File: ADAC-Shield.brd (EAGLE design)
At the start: 100 x 80 mm, 58 parts, among them U1 ARDUINO-MEGAFULL, U2 LM358D

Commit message: Some progress in PCB layout
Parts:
- removed R1: 0, rcl:R1206
- added JP4: (no value), pinhead:1X02
- moved C21 52.9 mm to (41.3, 26.0), turned to 270 degrees
- moved C25 50.7 mm to (52.1, 21.9), turned to 90 degrees
- moved R17 48.8 mm to (38.1, 22.5)
- moved C19 47.5 mm to (47.6, 31.4), turned to 270 degrees
- moved R19 45.3 mm to (57.8, 21.9), turned to 90 degrees
- moved C26 44.3 mm to (54.9, 21.6), turned to 90 degrees
- moved C23 41.9 mm to (52.7, 31.4), turned to 90 degrees
- moved C20 34.9 mm to (38.4, 26.0), turned to 270 degrees
- moved R18 34.9 mm to (58.4, 31.4), turned to 90 degrees
- moved C24 33.3 mm to (55.6, 31.8), turned to 270 degrees
- moved C22 28.0 mm to (44.8, 31.8), turned to 270 degrees
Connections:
- net +3V3: now also JP4.2; no longer R1.1
- net V+: now also JP4.1; no longer R1.2
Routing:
- net GND: track 54.6 -> 192.5 mm, vias 0 -> 2
- net V+: track 6.06 -> 46.9 mm, vias 0 -> 4
- net RIGHT_PREAMP_OUT: track 3.41 -> 17.9 mm, vias 0 -> 1
- net LEFT_PREAMP_OUT: track 3.41 -> 17.4 mm, vias 0 -> 1
- net N$19: track 0.00 -> 11.6 mm
- net N$20: track 0.00 -> 8.86 mm
- net N$25: track 0.00 -> 8.36 mm
- net N$18: track 0.00 -> 6.69 mm
- net +3V3: track 0.00 -> 2.86 mm, vias 0 -> 1

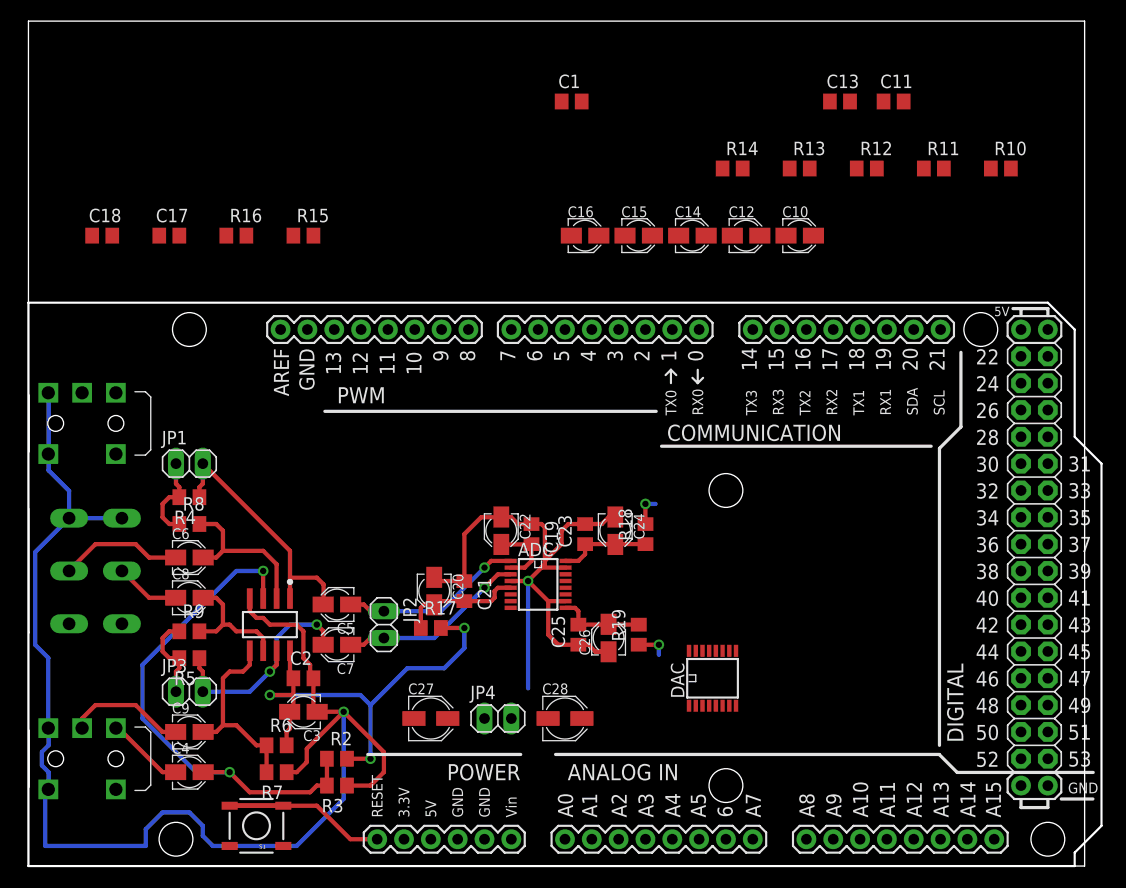
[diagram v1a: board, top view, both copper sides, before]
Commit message: PCB layout almost done
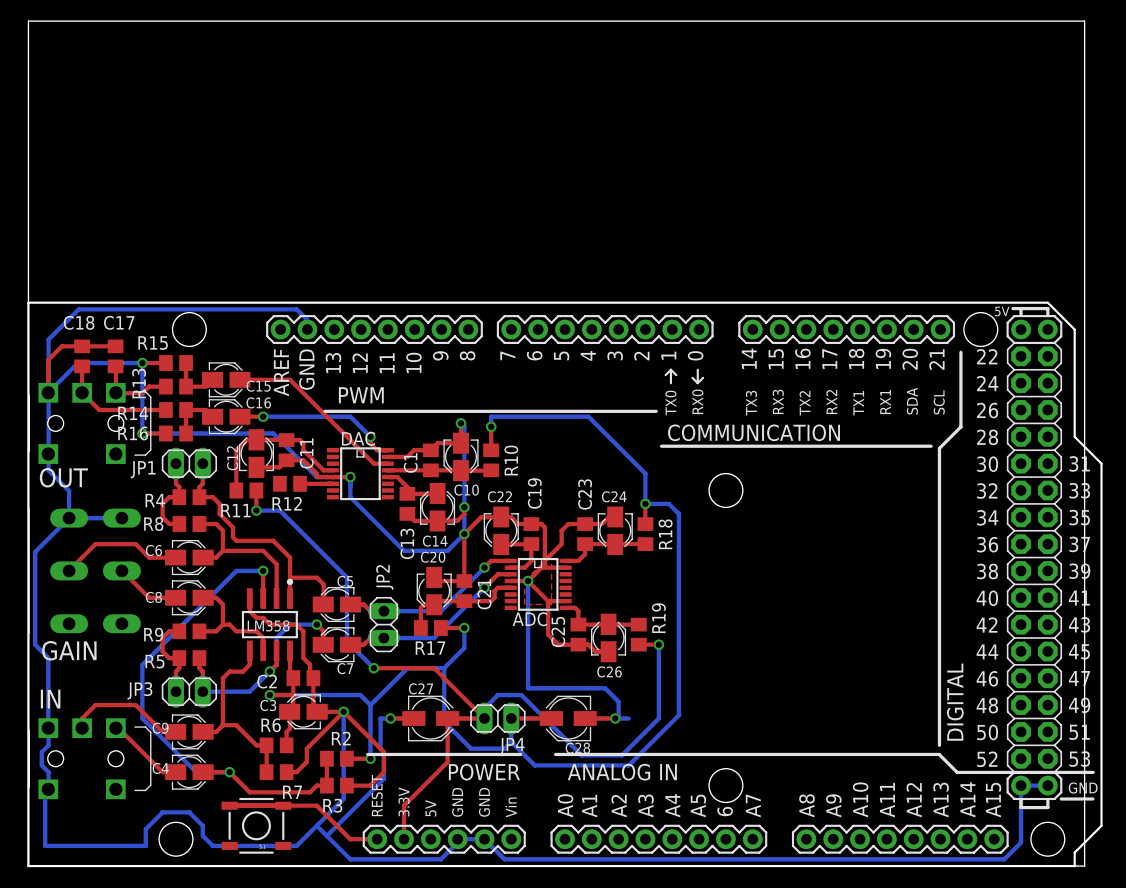
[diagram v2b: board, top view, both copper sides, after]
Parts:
- moved R11 71.9 mm to (20.6, 35.6)
- moved C11 66.3 mm to (24.4, 39.4), turned to 270 degrees
- moved R13 62.6 mm to (14.0, 45.4)
- moved R12 62.2 mm to (24.8, 36.2), turned to 180 degrees
- moved R14 57.4 mm to (14.0, 43.2)
- moved C13 55.9 mm to (35.9, 34.3), turned to 270 degrees
- moved R10 55.6 mm to (43.8, 38.4), turned to 90 degrees
- moved C12 50.7 mm to (21.6, 39.1), turned to 90 degrees
- moved C15 41.4 mm to (18.7, 46.0)
- moved DAC 38.6 mm to (31.4, 37.1), turned to 270 degrees
- moved C10 38.3 mm to (41.0, 38.7), turned to 270 degrees
- moved C16 38.1 mm to (18.7, 42.5)
- moved C1 36.5 mm to (38.1, 38.4), turned to 90 degrees
- moved C14 35.3 mm to (38.7, 34.0), turned to 90 degrees
- moved R16 19.6 mm to (14.0, 41.0), turned to 180 degrees
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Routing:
- net GND: track 192.5 -> 440.1 mm, vias 2 -> 10
- net V+: track 46.9 -> 129.0 mm, vias 4 -> 5
- net +3V3: track 2.86 -> 82.5 mm, vias 1 -> 3
- net N$14: track 0.00 -> 17.3 mm
- net N$15: track 0.00 -> 15.7 mm, vias 0 -> 2
- net N$6: track 0.00 -> 14.9 mm
- net RIGHT_DAC_OUT: track 0.00 -> 11.1 mm
- net N$10: track 0.00 -> 9.81 mm
- net LEFT_DAC_OUT: track 0.00 -> 7.53 mm
- net N$13: track 0.00 -> 5.75 mm
- net N$17: track 0.00 -> 5.00 mm
- net N$16: track 0.00 -> 5.00 mm
- net N$12: track 0.00 -> 3.12 mm
- added copper zone on layer 1, net GND
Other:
- board text added: "GAIN"
- board text added: "IN"
- board text added: "LM358"
- board text added: "OUT"

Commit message: Board layout finished for v0.1
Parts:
- U1: device SparkFun-Boards:ARDUINO_MEGA -> SparkFun-Boards_modified:ARDUINO_MEGA
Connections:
- net ADC_BCK: now also U1.45
- net ADC_DATAO: now also U1.47
- net ADC_MSSEL: now also U1.48
- net ADC_PWON: now also U1.50
- net ADC_SFOR: now also U1.51
- net ADC_SYSCLK: now also U1.49
- net ADC_WS: now also U1.46
- net DAC_BCK: now also U1.34
- net DAC_DATAI: now also U1.36
- net DAC_DEEM: now also U1.40
- net DAC_MUTE: now also U1.39
- net DAC_PCS: now also U1.41
- net DAC_SFOR0: now also U1.38
- net DAC_SFOR1: now also U1.37
- net DAC_SYSCLK: now also U1.33
- net DAC_WS: now also U1.35
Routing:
- net DAC_SYSCLK: track 0.00 -> 84.5 mm, vias 0 -> 2
- net DAC_WS: track 0.00 -> 82.3 mm, vias 0 -> 2
- net DAC_MUTE: track 0.00 -> 80.6 mm, vias 0 -> 2
- net DAC_PCS: track 0.00 -> 79.9 mm, vias 0 -> 2
- net DAC_SFOR1: track 0.00 -> 79.6 mm, vias 0 -> 2
- net DAC_SFOR0: track 0.00 -> 77.7 mm, vias 0 -> 2
- net DAC_BCK: track 0.00 -> 75.9 mm, vias 0 -> 2
- net DAC_DATAI: track 0.00 -> 75.6 mm, vias 0 -> 2
- net DAC_DEEM: track 0.00 -> 72.6 mm, vias 0 -> 2
- net ADC_SYSCLK: track 0.00 -> 64.1 mm
- net ADC_SFOR: track 0.00 -> 58.1 mm
- net ADC_WS: track 0.00 -> 57.6 mm
- net ADC_PWON: track 0.00 -> 55.3 mm
- net ADC_DATAO: track 0.00 -> 51.1 mm, vias 0 -> 1
- net ADC_MSSEL: track 0.00 -> 49.1 mm, vias 0 -> 1
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- added copper zone on layer 16, net GND
- removed copper zone on layer 1, net GND
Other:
- board size 100 x 80 mm -> 101.6 x 53.3 mm

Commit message: Small board fixes
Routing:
- net GND: track 417.8 -> 427.7 mm, vias 10 -> 11
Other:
- board text added: "ADAC v0.1"
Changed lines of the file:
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@@
 <wire x1="101.5875" y1="53.33" x2="0" y2="53.33" width="0" layer="20"/>
 <wire x1="0" y1="53.33" x2="0" y2="0" width="0" layer="20"/>
-<text x="0.9525" y="14.9225" size="1.778" layer="121">IN</text>
-<text x="0.9525" y="35.8775" size="1.778" layer="121">OUT</text>
-<text x="6.6675" y="21.2725" size="1.778" layer="121" rot="R180">GAIN</text>
-<text x="20.6375" y="22.225" size="1.016" layer="121">LM358</text>
+<text x="0.9525" y="14.9225" size="1.778" layer="25">IN</text>
+<text x="0.9525" y="35.8775" size="1.778" layer="25">OUT</text>
+<text x="6.6675" y="21.2725" size="1.778" layer="25" rot="R180">GAIN</text>
+<text x="20.6375" y="22.225" size="1.016" layer="25">LM358</text>
+<text x="66.04" y="20.32" size="2.54" layer="25">ADAC v0.1</text>
+<text x="66.04" y="20.32" size="2.54" layer="1">ADAC v0.1</text>
 </plain>
 <attributes>
@@
 </element>
 <element name="C15" library="rcl" package="PANASONIC_A" value="47" x="18.7325" y="46.0375" smashed="yes">
-<attribute name="NAME" x="20.575" y="44.93" size="1.016" layer="25"/>
+<attribute name="NAME" x="16.4475" y="47.7875" size="1.016" layer="25"/>
 </element>
 <element name="C16" library="rcl" package="PANASONIC_A" value="47" x="18.7325" y="42.545" smashed="yes">
-<attribute name="NAME" x="20.575" y="43.3425" size="1.016" layer="25"/>
+<attribute name="NAME" x="16.4475" y="39.85" size="1.016" layer="25"/>
 </element>
 <element name="R13" library="rcl" package="R0805" value="100" x="13.97" y="45.4025" smashed="yes">
@@
 <wire x1="29.845" y1="14.605" x2="29.845" y2="6.35" width="0.4064" layer="16"/>
 <wire x1="29.845" y1="6.35" x2="27.305" y2="3.81" width="0.4064" layer="16"/>
-<wire x1="27.305" y1="3.81" x2="25.4" y2="1.905" width="0.4064" layer="16"/>
+<wire x1="27.305" y1="3.81" x2="27.14625" y2="3.65125" width="0.4064" layer="16"/>
+<wire x1="27.14625" y1="3.65125" x2="25.4" y2="1.905" width="0.4064" layer="16"/>
 <wire x1="25.4" y1="1.905" x2="17.4625" y2="1.905" width="0.4064" layer="16"/>
 <wire x1="17.4625" y1="1.905" x2="16.51" y2="2.8575" width="0.4064" layer="16"/>
@@
 <wire x1="5.3975" y1="39.0525" x2="5.3975" y2="41.2925" width="0.4064" layer="16"/>
 <wire x1="5.3975" y1="41.2925" x2="1.88" y2="44.81" width="0.4064" layer="16"/>
-<wire x1="25.4" y1="1.905" x2="24.13" y2="1.905" width="0" layer="19" extent="1-16"/>
-<wire x1="19.05" y1="1.905" x2="17.4625" y2="1.905" width="0" layer="19" extent="1-16"/>
+<wire x1="19.05" y1="1.905" x2="24.13" y2="1.905" width="0.4064" layer="1"/>
+<wire x1="24.13" y1="1.905" x2="25.4" y2="1.905" width="0.4064" layer="1"/>
+<wire x1="25.4" y1="1.905" x2="25.7175" y2="2.2225" width="0.4064" layer="1"/>
+<wire x1="25.7175" y1="2.2225" x2="25.7175" y2="3.81" width="0.4064" layer="1"/>
+<via x="25.7175" y="3.81" extent="1-16" drill="0.6" shape="octagon"/>
+<wire x1="25.7175" y1="3.81" x2="26.9875" y2="3.81" width="0.4064" layer="16"/>
+<wire x1="26.9875" y1="3.81" x2="27.14625" y2="3.65125" width="0.4064" layer="16"/>
+<wire x1="1.905" y1="7.3025" x2="1.905" y2="13.035" width="0" layer="19" extent="16-16"/>
 </signal>
 <signal name="N$3">
